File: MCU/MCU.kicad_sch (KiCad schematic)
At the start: 4 parts, among them J1 Conn_01x02, J2 Conn_01x02, J3 Conn_01x02, U1 Nucleo_L432KC

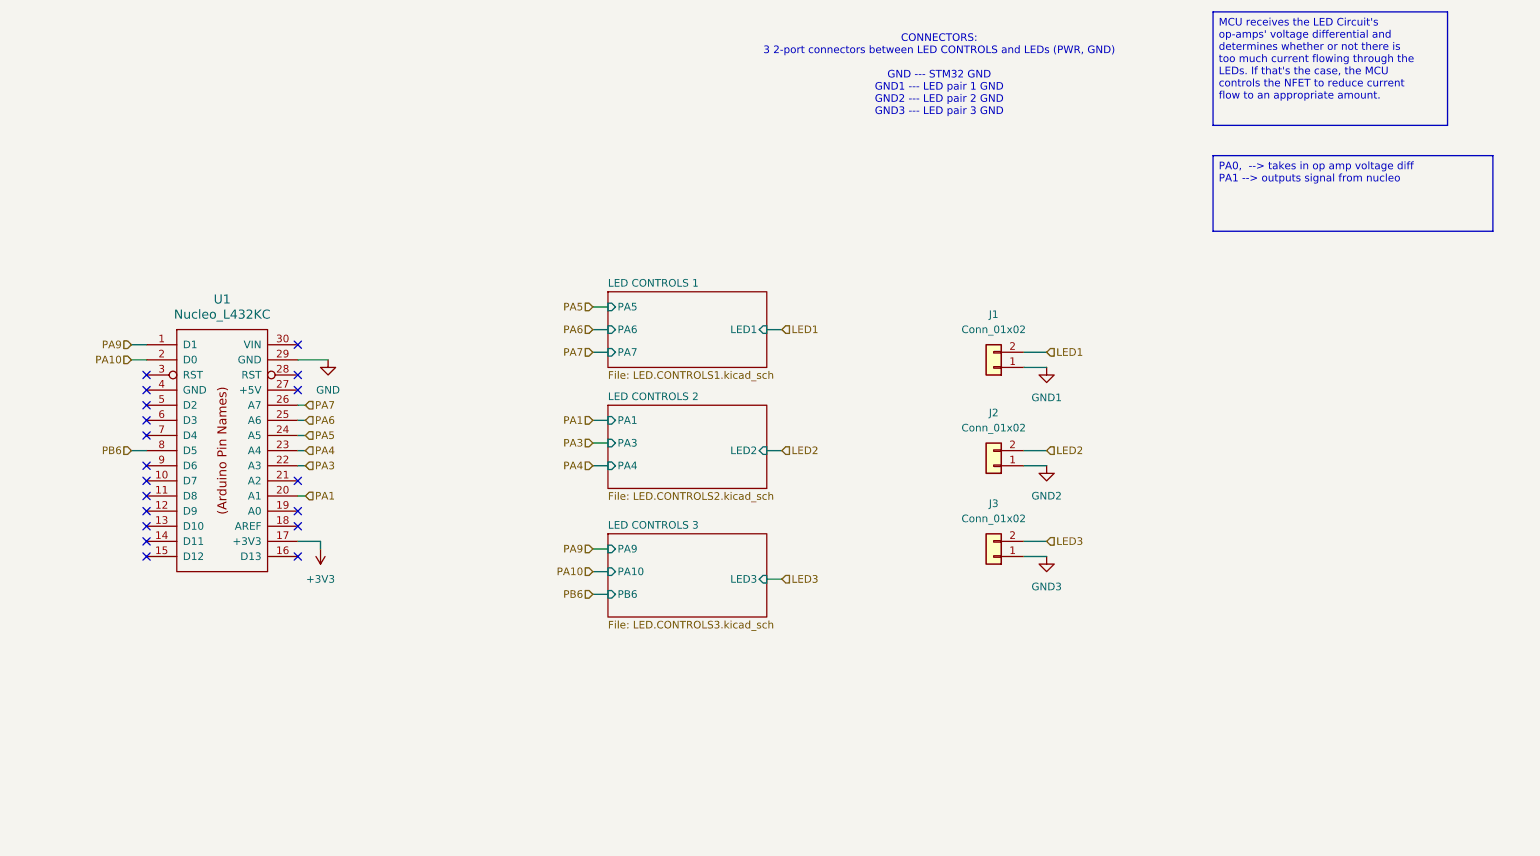
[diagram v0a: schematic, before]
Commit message: Centralized isolation amp power source. Corrected STM32 pins.
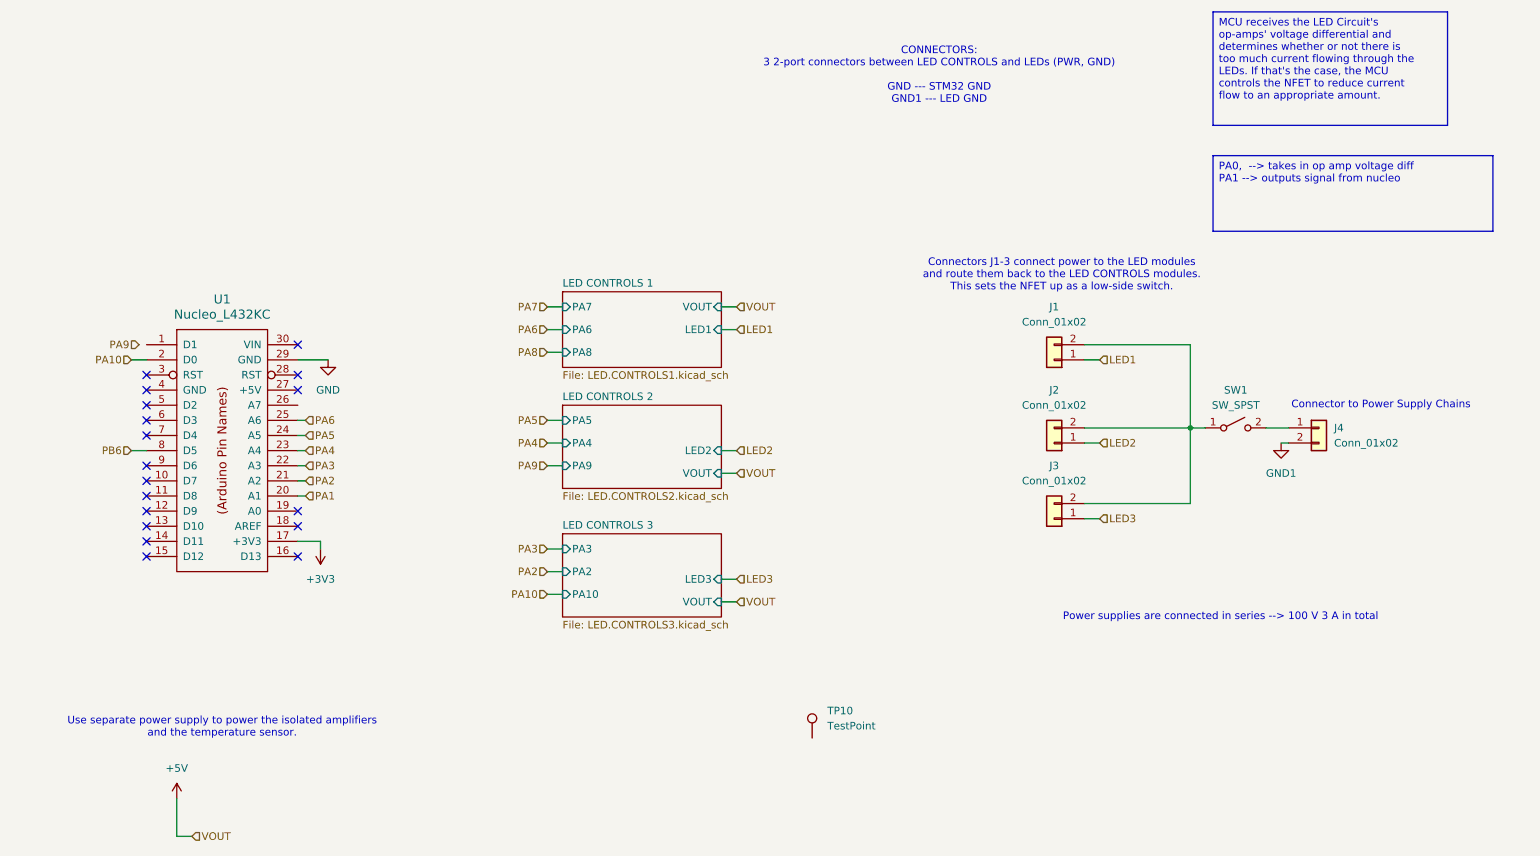
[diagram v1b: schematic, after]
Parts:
- added J4: Conn_01x02, symbol Connector_Generic:Conn_01x02
- added SW1: SW_SPST, symbol Switch:SW_SPST
- added TP10: TestPoint, symbol Connector:TestPoint
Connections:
- net GND2 is gone; now on net LED2: J2.1 (Pin_1)
- net GND3 is gone; now on net LED3: J3.1 (Pin_1)
- net GND1: now also J4.2 (Pin_2); no longer J1.1 (Pin_1)
- net LED1: now also J1.1 (Pin_1); no longer J1.2 (Pin_2)
- net LED2: no longer J2.2 (Pin_2)
- net LED3: no longer J3.2 (Pin_2)
- net PA7: no longer U1.26 (A7)
- net PA9: no longer U1.1 (D1)
- net PA2: now reaches U1.21 (A2)
- new net: J1.2 (Pin_2), J2.2 (Pin_2), J3.2 (Pin_2), SW1.1 (A)
- new net: J4.1 (Pin_1), SW1.2 (B)
- no-connect marks 19 -> 18
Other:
- sheet LED CONTROLS 1 ports: added PA8, VOUT; removed PA5
- sheet LED CONTROLS 2 ports: added PA5, PA9, VOUT; removed PA1, PA3
- sheet LED CONTROLS 3 ports: added PA2, PA3, VOUT; removed PA9, PB6
- note added: "CONNECTORS: 3 2-port connectors between LED CONTROLS and LEDs (PWR, GND) GND --- STM32 GND GND1 --- LED GND"
- note added: "Connector to Power Supply Chains"
- note added: "Connectors J1-3 connect power to the LED modules and route them back to the LED CONTROLS modules. This sets the NFET up as a low-side switch."
- note added: "Power supplies are connected in series --> 100 V 3 A in total"
- note added: "Use separate power supply to power the isolated amplifiers and the temperature sensor."
- note removed: "CONNECTORS: 3 2-port connectors between LED CONTROLS and LEDs (PWR, GND) GND --- STM32 GND GND1 --- LED pair 1 GND GND2 --- LED pair 2 GND GND3 --- LED pair 3 GND"

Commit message: Assigned footprints and added RTD
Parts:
- removed SW1: SW_SPST, symbol Switch:SW_SPST
- removed TP10: TestPoint, symbol Connector:TestPoint
- added J5: Conn_01x02, Connector_Molex:Molex_CLIK-Mate_502382-0270_1x02-1MP_P1.25mm_Vertical, symbol Connector_Generic:Conn_01x02
- added SW2: SW_Push, symbol Switch:SW_Push
- J1, J2, J3, J4: footprint (none) -> Connector_Molex:Molex_CLIK-Mate_502382-0270_1x02-1MP_P1.25mm_Vertical
- U1: footprint (none) -> STM32_L432KC Nucleo:UFQFPN-32
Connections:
- net GND1: now also J5.1 (Pin_1)
- net Buck_100_5V/VIN: now reaches J1.2 (Pin_2), J2.2 (Pin_2), J3.2 (Pin_2)
- net Buck_100_5V/VIN: now also SW2.1
- net at J4.1 (Pin_1): now also SW2.2
- net PA0: now reaches U1.19 (A0)
- net PB0: now reaches U1.6 (D3)
- new net +RTD: J5.2 (Pin_2)
- no-connect marks 18 -> 16
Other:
- added sheet Buck_100_5V (untitled.kicad_sch)
- added sheet RTD CONTROLS (RTDControls.kicad_sch)
- note added: "Connector to RTD"
- note removed: "Use separate power supply to power the isolated amplifiers and the temperature sensor."

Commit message: Finalized schematic and started layout
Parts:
- removed SW2: SW_Push, symbol Switch:SW_Push
- added R1: 7.5, Resistor_SMD:R_0402_1005Metric_Pad0.72x0.64mm_HandSolder, symbol Device:R
- U1: footprint STM32_L432KC Nucleo:UFQFPN-32 -> UTSVT Special:NucleoL432KC
- renumbered J5 to J1, J1 to J2, J2 to J3, J3 to J4, J4 to J5
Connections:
- net Buck_100_5V/VIN is gone; now on an unnamed net: J2.2 (Pin_2), J3.2 (Pin_2), J4.2 (Pin_2)
- net PA9: now also U1.1 (D1)
- net D7: now reaches U1.10 (D7)
- net D8: now reaches U1.11 (D8)
- net D9: now reaches U1.12 (D9)
- net +5V: now reaches U1.27 (+5V)
- net +5V: now also R1.1
- net +RTD renamed RTD
- net RTD: now also R1.2
- no-connect marks 16 -> 13
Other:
- removed sheet Buck_100_5V
- sheet LED CONTROLS 1 ports: added CTRL, DIAG, LED_IN, VOUTN, VOUTP; removed LED1, PA6, PA7, PA8, VOUT
- sheet LED CONTROLS 2: file LED.CONTROLS2.kicad_sch -> LED.CONTROLS1.kicad_sch
- sheet LED CONTROLS 2 ports: added CTRL, DIAG, LED_IN, VOUTN, VOUTP; removed LED2, PA4, PA5, PA9, VOUT
- sheet LED CONTROLS 3: file LED.CONTROLS3.kicad_sch -> LED.CONTROLS1.kicad_sch
- sheet LED CONTROLS 3 ports: added CTRL, DIAG, LED_IN, VOUTN, VOUTP; removed LED3, PA10, PA2, PA3, VOUT
- sheet RTD CONTROLS ports: added none; removed VOUT
- note added: "Power supplies are connected in parallel --> 100 V 3 A in total"
- note added: "what does DIAG specifically output? need to know if i need ADC"
- note removed: "Power supplies are connected in series --> 100 V 3 A in total"
- moved on the sheet: J1

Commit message: MCU Layout V1
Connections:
- net GND: now also J1.1 (Pin_1)
- net GND1: no longer J1.1 (Pin_1)
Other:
- note removed: "what does DIAG specifically output? need to know if i need ADC"
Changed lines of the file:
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@@
-		)
-	)
-	(text "what does DIAG specifically output? need to know if i need ADC\n"
-		(exclude_from_sim no)
-		(at 139.192 50.8 0)
-		(effects
-			(font
-				(size 1.27 1.27)
-			)
 		)
 	)
@@
 		)
 	)
-	(label "PA3"
+	(label "PA2"
 		(at 123.19 104.14 180)
 		(effects
@@
 		)
 	)
-	(label "PA10"
+	(label "PA1"
 		(at 123.19 111.76 180)
 		(effects
@@
 		)
 	)
-	(label "PA1"
+	(label "PA9"
 		(at 123.19 71.12 180)
 		(effects
@@
 		)
 	)
-	(label "PA6"
+	(label "PA10"
 		(at 123.19 67.31 180)
 		(effects
@@
 		)
 	)
+	(label "PA6"
+		(at 123.19 86.36 180)
+		(effects
+			(font
+				(size 1.27 1.27)
+			)
+			(justify right bottom)
+		)
+	)
 	(label "PA4"
-		(at 123.19 86.36 180)
-		(effects
-			(font
-				(size 1.27 1.27)
-			)
-			(justify right bottom)
-		)
-	)
-	(label "PA9"
 		(at 123.19 90.17 180)
 		(effects
@@
 		)
 	)
-	(label "PA2"
+	(label "PA3"
 		(at 123.19 107.95 180)
 		(effects
@@
 			)
 		)
-		(property "Value" "GND1"
+		(property "Value" "GND"
 			(at 219.71 139.7 0)
 			(effects

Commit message: Adjusted trace widths. Added ferrite beads. Changed connectors to fit new trace widths. Added +3V3 fill zone in B.Cu. Fixed silkscreen placements.
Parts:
- J2, J3, J4, J5: footprint Connector_Molex:Molex_CLIK-Mate_502382-0270_1x02-1MP_P1.25mm_Vertical -> Connector_JST:JST_VH_B2P-VH_1x02_P3.96mm_Vertical
- R1: value 7.5 -> 360; footprint Resistor_SMD:R_0402_1005Metric_Pad0.72x0.64mm_HandSolder -> Resistor_SMD:R_0805_2012Metric_Pad1.20x1.40mm_HandSolder
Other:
- note added: "Buy 2 extra 360 ohm resistors so I can test lead resistance error to increase RTD accuracy"
- note added: "RTD is PTS 0603 from VISHAY"

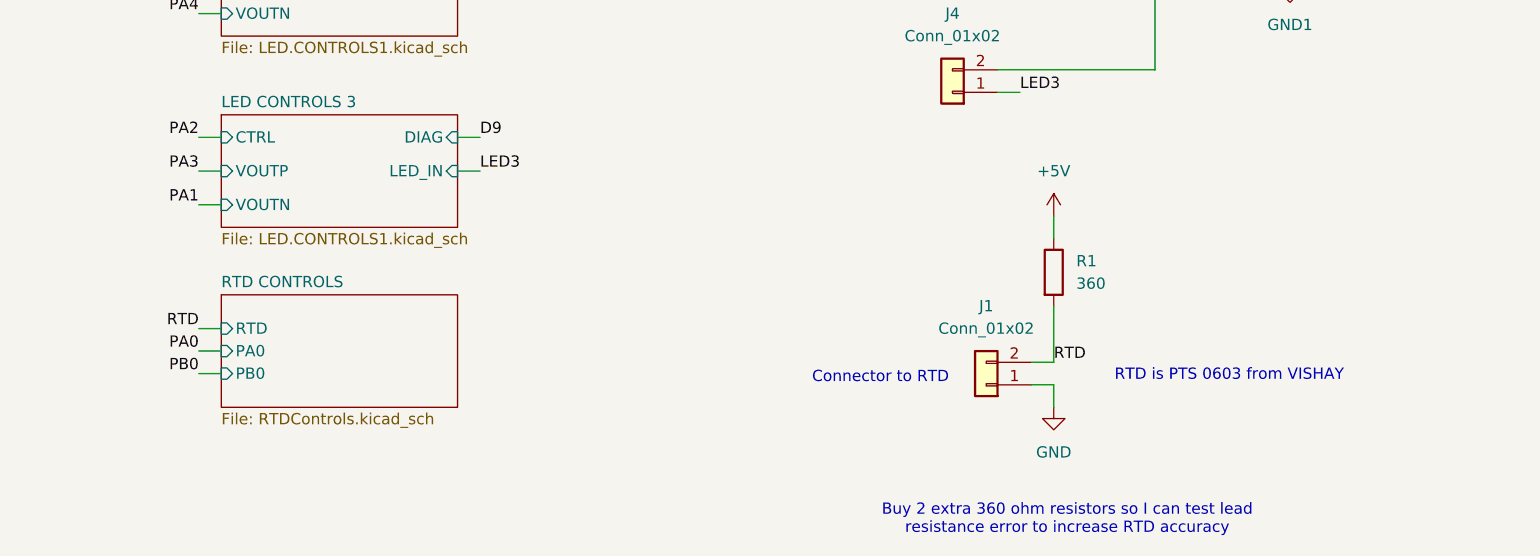
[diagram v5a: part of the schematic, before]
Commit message: Finished RTD schematic and layout. Got rid of RTD part of MCU.
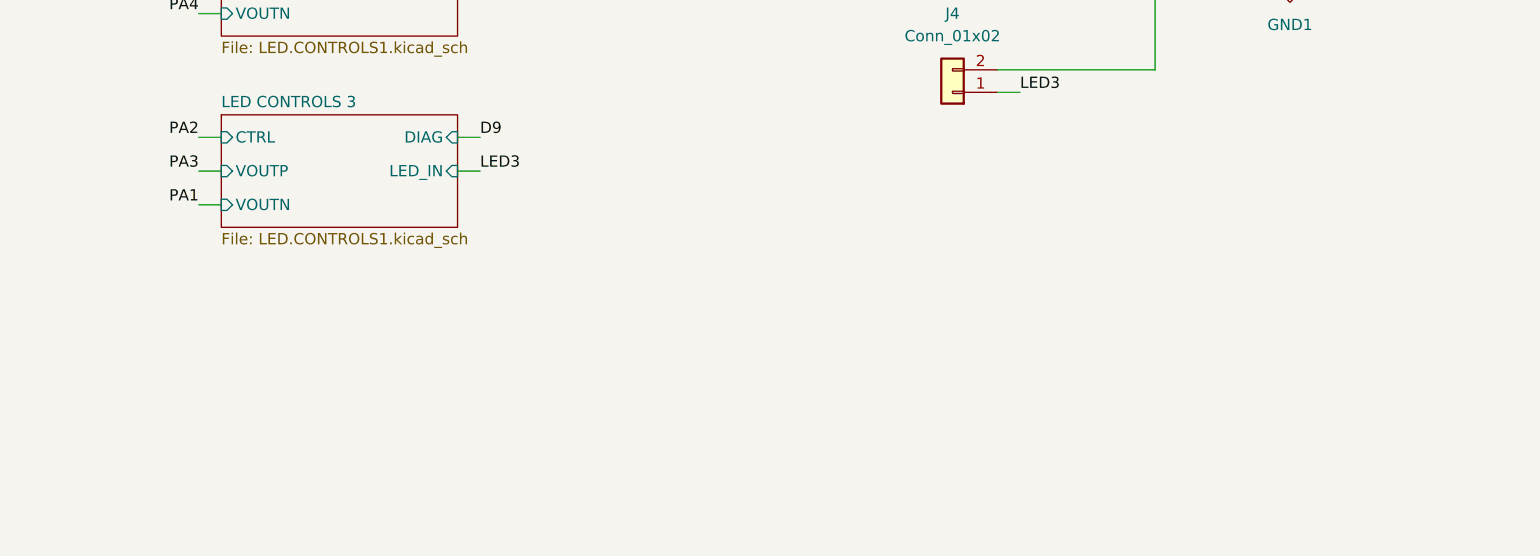
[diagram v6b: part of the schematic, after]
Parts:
- removed J1: Conn_01x02, Connector_Molex:Molex_CLIK-Mate_502382-0270_1x02-1MP_P1.25mm_Vertical, symbol Connector_Generic:Conn_01x02
- removed R1: 360, Resistor_SMD:R_0805_2012Metric_Pad1.20x1.40mm_HandSolder, symbol Device:R
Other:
- removed sheet RTD CONTROLS
- note removed: "Buy 2 extra 360 ohm resistors so I can test lead resistance error to increase RTD accuracy"
- note removed: "Connector to RTD"
- note removed: "RTD is PTS 0603 from VISHAY"

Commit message: layout suggestions
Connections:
- net +100V: now reaches J2.2 (Pin_2), J3.2 (Pin_2), J4.2 (Pin_2), J5.1 (Pin_1)
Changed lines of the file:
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@@
+	)
+	(junction
+		(at 237.49 83.82)
+		(diameter 0)
+		(color 0 0 0 0)
 	)
 	(junction
@@
 	(wire
 		(pts
+			(xy 237.49 83.82) (xy 247.65 83.82)
+		)
+		(stroke
+			(width 0)
+			(type default)
+		)
+	)
+	(wire
+		(pts
 			(xy 123.19 82.55) (xy 125.73 82.55)
 		)
@@
 	(wire
 		(pts
-			(xy 231.14 83.82) (xy 247.65 83.82)
+			(xy 231.14 83.82) (xy 237.49 83.82)
 		)
 		(stroke
@@
 		)
 	)
+	(symbol
+		(lib_id "power:+24V")
+		(at 237.49 83.82 0)
+		(unit 1)
+		(exclude_from_sim no)
+		(in_bom yes)
+		(on_board yes)
+		(dnp no)
+		(fields_autoplaced yes)
+		(property "Reference" "#PWR04"
+			(at 237.49 87.63 0)
+			(effects
+				(font
+					(size 1.27 1.27)
+				)
+				(hide yes)
+			)
+		)
+		(property "Value" "+100V"
+			(at 237.49 78.74 0)
+			(effects
+				(font
+					(size 1.27 1.27)
+				)
+			)
+		)
+		(property "Footprint" ""
+			(at 237.49 83.82 0)
+			(effects
+				(font
+					(size 1.27 1.27)
+				)
+				(hide yes)
+			)
+		)
+		(property "Datasheet" ""
+			(at 237.49 83.82 0)
+			(effects
+				(font
+					(size 1.27 1.27)
+				)
+				(hide yes)
+			)
+		)
+		(property "Description" "Power symbol creates a global label with name \"+24V\""
+			(at 237.49 83.82 0)
+			(effects
+				(font
+					(size 1.27 1.27)
+				)
+				(hide yes)
+			)
+		)
+		(pin "1"
+		)
+		(instances
+			(project ""
+				(path "/56b3f3ef-07ec-480e-b5f8-5a7fd51b01f6"
+					(reference "#PWR04")
+					(unit 1)
+				)
+			)
+		)
+	)

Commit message: layout changes
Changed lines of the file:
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@@
 	)
 	(label "PA2"
-		(at 123.19 104.14 180)
+		(at 106.68 99.06 180)
 		(effects
 			(font
@@
 	)
 	(label "PA1"
-		(at 123.19 111.76 180)
+		(at 123.19 107.95 180)
 		(effects
 			(font
@@
 		)
 	)
-	(label "PA5"
-		(at 123.19 82.55 180)
+	(label "PA3"
+		(at 123.19 90.17 180)
 		(effects
 			(font
@@
 	)
 	(label "PA6"
+		(at 111.76 78.74 180)
+		(effects
+			(font
+				(size 1.27 1.27)
+			)
+			(justify right bottom)
+		)
+	)
+	(label "PA2"
 		(at 123.19 86.36 180)
 		(effects
@@
 		)
 	)
-	(label "PA4"
-		(at 123.19 90.17 180)
+	(label "PA0"
+		(at 123.19 111.76 180)
 		(effects
 			(font
-				(size 1.27 1.27)
-			)
-			(justify right bottom)
-		)
-	)
-	(label "PA3"
-		(at 123.19 107.95 180)
-		(effects
-			(font
